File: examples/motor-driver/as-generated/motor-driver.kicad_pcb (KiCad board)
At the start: 2 copper layers, 100 x 50 mm, 12 parts, among them J1 VM 2.7-10.8V, J2 MOTOR A, J3 MOTOR B, J4 LOGIC, U1 DRV8833PW

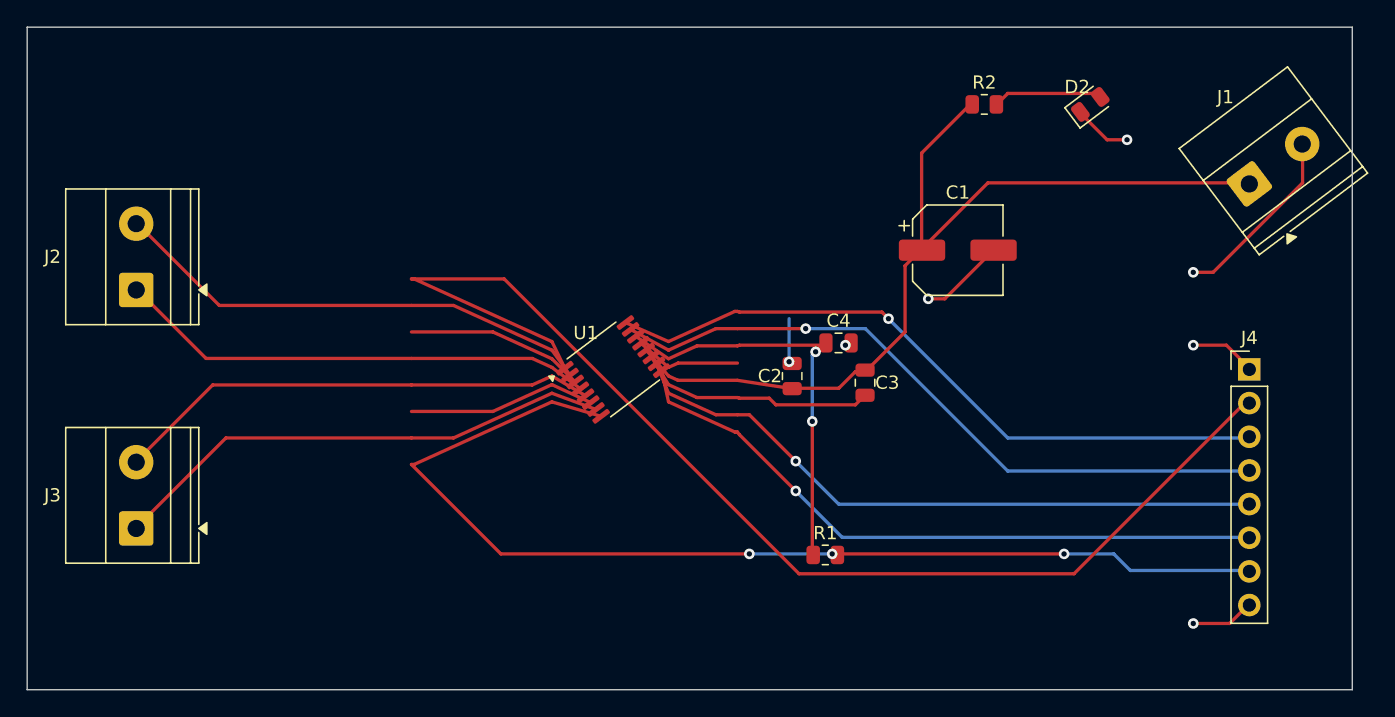
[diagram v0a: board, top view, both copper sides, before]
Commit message: Finish the fifth example, and stamp the model that wrote them
All five reviewed boards now pass KiCad's own checks: no DRC errors, nothing
unconnected, no schematic-parity findings, on 9.0.9 and 10.0.4. What is left
across the whole set is four silkscreen warnings and one library-footprint
hash, all of which come from the KiCad footprints themselves.

Getting the iCE40 board there found five things, each of which was silently
producing a board that was not the board the schematic described:

* **Two nets touching on the sheet is not something an endpoint check can
  see.** A wire that ends *on* another wire joins them, and on a sheet where
  every pin drags a stub behind it that is the common case. `schematic_shorts`
  looks for it now, and found three on this design - one of which had merged
  the 1.2 V and 3.3 V rails. The only visible sign had been KiCad's parity
  check disagreeing about a net name.
* **A symbol drawn in four units has to be placed four times.** Emitting all
  forty-eight pins under `(unit 1)` leaves three quarters of them in units
  that were never placed, which is twenty-five parity findings and a sheet
  nobody can read. The iCE40's banks and its supplies are four boxes now.
* **A pin the design does not use still has a net.** KiCad names it
  `unconnected-(U1A-IOT_37a-Pad23)`; a board that leaves the pad bare disagrees
  about every one of them.
* **A QFN counts anticlockwise**, so its east and north rows run bottom-to-top
  and right-to-left, and handing them to the fan-out in number order made
  every escape on those sides cross every other one.
* **Two rectangles that meet at a corner are further apart than growing both
  and asking whether they intersect makes them look** - which is every pair of
  pads on the corner of a QFN.

And two smaller ones: the router now keeps its vias away from every drilled
hole rather than only from its own, and the degraded variant is degraded from
the *routed* design rather than re-routed, which is both th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
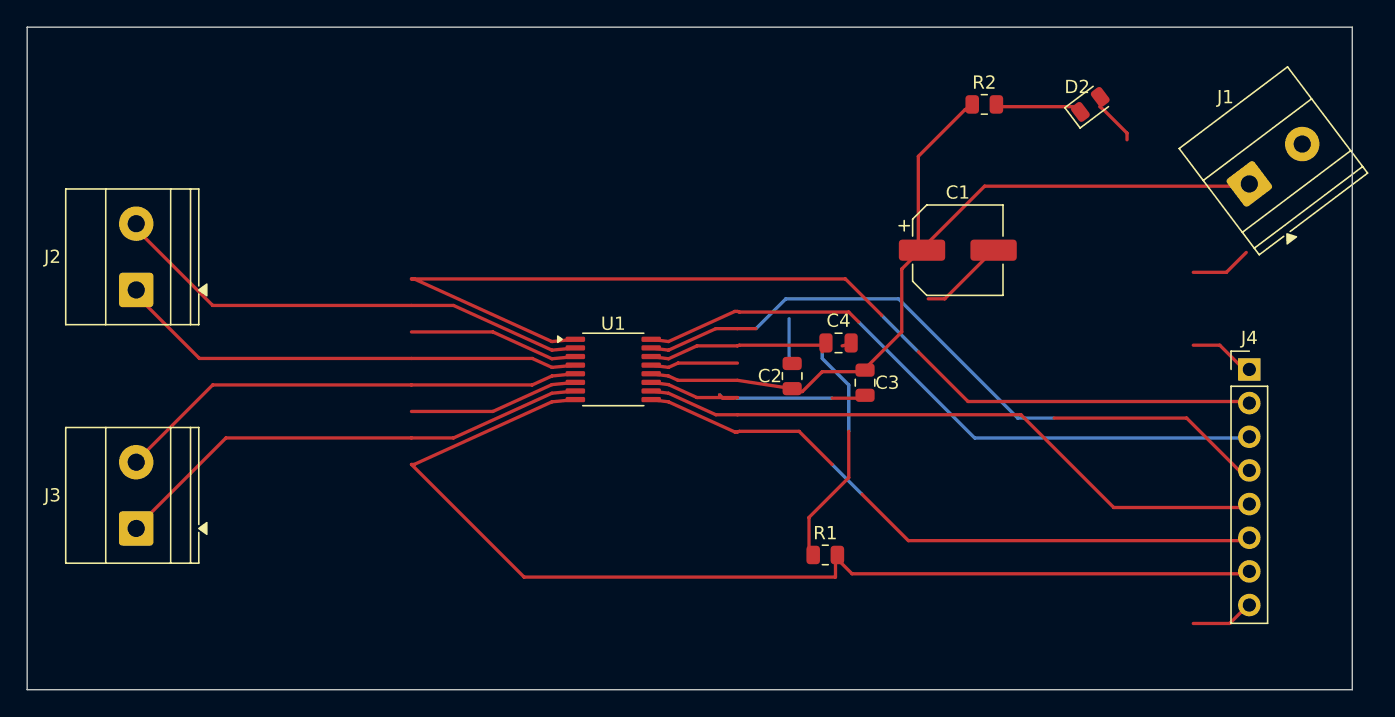
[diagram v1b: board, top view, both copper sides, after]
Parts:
- turned U1 to 0 degrees
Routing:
- net GND: track 74.7 -> 59.7 mm, vias 7 -> 0
- net /nSLEEP: track 91.7 -> 80.4 mm
- net /AIN1: track 51.8 -> 49.4 mm, vias 1 -> 0
- net /LED_A: track 8.29 -> 6.15 mm
- net /BOUT1: track 38.5 -> 37.0 mm
- net /VM: track 68.5 -> 67.1 mm
- net /BIN1: track 50.0 -> 48.8 mm, vias 1 -> 0
- net /BIN2: track 49.4 -> 48.2 mm, vias 1 -> 0
- net /VCP: track 18.0 -> 19.0 mm
- net /BOUT2: track 36.9 -> 36.0 mm
- net /AOUT2: track 36.3 -> 35.6 mm
- net /VINT: track 31.6 -> 31.3 mm, vias 2 -> 0
- net /AIN2: track 51.9 -> 51.6 mm, vias 1 -> 0
- net /nFAULT: track 82.1 -> 82.0 mm, vias 3 -> 0
